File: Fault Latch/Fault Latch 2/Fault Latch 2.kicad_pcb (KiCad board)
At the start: 2 copper layers, 9 parts, among them K103 Fujitsu_FTR-LYAA005x, K104 Fujitsu_FTR-LYAA005x, K105 Fujitsu_FTR-LYAA005x, SW1 SW_Omron_B3FS, SW2 SW_Omron_B3FS, SW3 SW_Omron_B3FS, U105 SFH617A-1, U108 SFH617A-1, U111 SFH617A-1

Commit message: Fault Latch Overhaul
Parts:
- removed SW1, SW2, SW3: SW_Omron_B3FS, Button_Switch_SMD:SW_SPST_Omron_B3FS-100xP
- added C101: 10n, Capacitor_SMD:C_0603_1608Metric_Pad1.08x0.95mm_HandSolder, F.Cu at (94.2, 101.5)
- added C102: 100n, Capacitor_SMD:C_0603_1608Metric_Pad1.08x0.95mm_HandSolder, F.Cu at (88.2, 78.2)
- added C103: 100n, Capacitor_SMD:C_0603_1608Metric_Pad1.08x0.95mm_HandSolder, F.Cu at (95.0, 78.2)
- added C104: 100n, Capacitor_SMD:C_0603_1608Metric_Pad1.08x0.95mm_HandSolder, F.Cu at (81.2, 78.2)
- added C105: 10n, Capacitor_SMD:C_0603_1608Metric_Pad1.08x0.95mm_HandSolder, F.Cu at (94.2, 118.2)
- added C106: 10n, Capacitor_SMD:C_0603_1608Metric_Pad1.08x0.95mm_HandSolder, F.Cu at (93.9, 134.8)
- added C107: 47u, Capacitor_SMD:CP_Elec_6.3x5.4, F.Cu at (133.0, 138.4)
- added C108: 1u, Capacitor_SMD:C_0805_2012Metric_Pad1.18x1.45mm_HandSolder, F.Cu at (115.0, 136.5)
- added C109: 0.33u, Capacitor_SMD:C_0603_1608Metric_Pad1.08x0.95mm_HandSolder, F.Cu at (115.0, 134.5)
- added C110: 100n, Capacitor_SMD:C_0603_1608Metric_Pad1.08x0.95mm_HandSolder, F.Cu at (104.6, 135.5)
- added C111: 100n, Capacitor_SMD:C_0603_1608Metric_Pad1.08x0.95mm_HandSolder, F.Cu at (85.3, 66.4)
- added D101: RED, LED_SMD:LED_0805_2012Metric_Pad1.15x1.40mm_HandSolder, F.Cu at (103.4, 113.0)
- added D102: RED, LED_SMD:LED_0805_2012Metric_Pad1.15x1.40mm_HandSolder, F.Cu at (103.4, 104.0)
- added D103: RED, LED_SMD:LED_0805_2012Metric_Pad1.15x1.40mm_HandSolder, F.Cu at (103.5, 94.8)
- added D104: D_Schottky, Diode_SMD:D_SMA, F.Cu at (135.0, 56.0)
- added D105: D_Schottky, Diode_SMD:D_SMA, F.Cu at (135.5, 67.2)
- added D106: D_Schottky, Diode_SMD:D_SMA, F.Cu at (135.2, 78.8)
- added H101: MountingHole, MountingHole:MountingHole_3.2mm_M3, F.Cu at (80.0, 145.0)
- added H102: MountingHole, MountingHole:MountingHole_3.2mm_M3, F.Cu at (175.0, 145.0)
- added H103: MountingHole, MountingHole:MountingHole_3.2mm_M3, F.Cu at (175.0, 55.0)
- added H104: MountingHole, MountingHole:MountingHole_3.2mm_M3, F.Cu at (80.0, 55.0)
- added PS101: RI-1205S, DC-DC:RI0505S, F.Cu at (114.3, 140.5)
- added Q104: Q_NPN_BEC, Package_TO_SOT_SMD:SOT-23, F.Cu at (90.0, 104.3)
- added Q106: Q_NPN_BEC, Package_TO_SOT_SMD:SOT-23, F.Cu at (94.0, 98.8)
- added Q107: Q_NPN_BEC, Package_TO_SOT_SMD:SOT-23, F.Cu at (89.8, 121.0)
- added Q108: Q_NPN_BEC, Package_TO_SOT_SMD:SOT-23, F.Cu at (94.0, 115.5)
- added Q109: Q_NMOS_GDS, Package_TO_SOT_SMD:TO-252-2, F.Cu at (125.0, 61.2)
- added Q110: Q_NMOS_GDS, Package_TO_SOT_SMD:TO-252-2, F.Cu at (125.1, 70.7)
- added Q111: Q_NMOS_GDS, Package_TO_SOT_SMD:TO-252-2, F.Cu at (125.1, 80.8)
- added Q112: Q_NPN_BEC, Package_TO_SOT_SMD:SOT-23, F.Cu at (89.8, 137.5)
- added Q113: Q_NPN_BEC, Package_TO_SOT_SMD:SOT-23, F.Cu at (93.8, 132.0)
- added R101: 100k, Resistor_SMD:R_0805_2012Metric_Pad1.20x1.40mm_HandSolder, F.Cu at (84.5, 104.3)
- added R102: 10k, Resistor_SMD:R_0805_2012Metric_Pad1.20x1.40mm_HandSolder, F.Cu at (86.8, 104.3)
- added R104: 270R, Resistor_SMD:R_0805_2012Metric_Pad1.20x1.40mm_HandSolder, F.Cu at (100.9, 113.0)
- added R105: 270R, Resistor_SMD:R_0805_2012Metric_Pad1.20x1.40mm_HandSolder, F.Cu at (100.9, 104.0)
- added R106: 1k, Resistor_SMD:R_0805_2012Metric_Pad1.20x1.40mm_HandSolder, F.Cu at (93.2, 104.3)
- added R107: 270R, Resistor_SMD:R_0805_2012Metric_Pad1.20x1.40mm_HandSolder, F.Cu at (101.0, 94.8)
- added R108: 100k, Resistor_SMD:R_0805_2012Metric_Pad1.20x1.40mm_HandSolder, F.Cu at (95.5, 104.3)
- added R109: 1k, Resistor_SMD:R_0805_2012Metric_Pad1.20x1.40mm_HandSolder, F.Cu at (90.8, 97.8)
- added R112: 100k, Resistor_SMD:R_0805_2012Metric_Pad1.20x1.40mm_HandSolder, F.Cu at (84.3, 121.0)
- added R113: 10k, Resistor_SMD:R_0805_2012Metric_Pad1.20x1.40mm_HandSolder, F.Cu at (86.8, 121.0)
- added R114: 1k, Resistor_SMD:R_0805_2012Metric_Pad1.20x1.40mm_HandSolder, F.Cu at (93.0, 121.0)
- added R115: 100k, Resistor_SMD:R_0805_2012Metric_Pad1.20x1.40mm_HandSolder, F.Cu at (95.2, 121.0)
- added R116: 270R, Resistor_SMD:R_0805_2012Metric_Pad1.20x1.40mm_HandSolder, F.Cu at (105.7, 57.4)
- added R117: 270R, Resistor_SMD:R_0805_2012Metric_Pad1.20x1.40mm_HandSolder, F.Cu at (105.7, 67.0)
- added R118: 270R, Resistor_SMD:R_0805_2012Metric_Pad1.20x1.40mm_HandSolder, F.Cu at (105.7, 76.8)
- added R120: 1k, Resistor_SMD:R_0805_2012Metric_Pad1.20x1.40mm_HandSolder, F.Cu at (90.8, 114.5)
- added R121: 10k, Resistor_SMD:R_0805_2012Metric_Pad1.20x1.40mm_HandSolder, F.Cu at (115.3, 57.4)
- added R122: 10k, Resistor_SMD:R_0805_2012Metric_Pad1.20x1.40mm_HandSolder, F.Cu at (115.3, 67.0)
- added R123: 10k, Resistor_SMD:R_0805_2012Metric_Pad1.20x1.40mm_HandSolder, F.Cu at (115.3, 76.8)
- added R124: 100k, Resistor_SMD:R_0805_2012Metric_Pad1.20x1.40mm_HandSolder, F.Cu at (84.0, 137.6)
- added R125: 10k, Resistor_SMD:R_0805_2012Metric_Pad1.20x1.40mm_HandSolder, F.Cu at (86.5, 137.6)
- added R126: 1k, Resistor_SMD:R_0805_2012Metric_Pad1.20x1.40mm_HandSolder, F.Cu at (92.8, 137.5)
- added R127: 100k, Resistor_SMD:R_0805_2012Metric_Pad1.20x1.40mm_HandSolder, F.Cu at (94.9, 137.5)
- added R128: 1k, Resistor_SMD:R_0805_2012Metric_Pad1.20x1.40mm_HandSolder, F.Cu at (90.5, 131.0)
- added R129: 10k, Resistor_SMD:R_0805_2012Metric_Pad1.20x1.40mm_HandSolder, F.Cu at (117.0, 96.8)
- added R131: 2.2k, Resistor_SMD:R_0805_2012Metric_Pad1.20x1.40mm_HandSolder, F.Cu at (117.0, 112.8)
- added R135: 10k, Resistor_SMD:R_0805_2012Metric_Pad1.20x1.40mm_HandSolder, F.Cu at (117.0, 103.8)
- added SW101: SW_Omron_B3FS, Button_Switch_SMD:SW_SPST_Omron_B3FS-100xP, F.Cu at (84.5, 96.8)
- added SW102: SW_Omron_B3FS, Button_Switch_SMD:SW_SPST_Omron_B3FS-100xP, F.Cu at (84.5, 113.2)
- added SW103: SW_Omron_B3FS, Button_Switch_SMD:SW_SPST_Omron_B3FS-100xP, F.Cu at (84.2, 130.0)
- added U101: 641964-1, 641964-1:TE_641964-1, F.Cu at (135.0, 98.8)
- added U102: 74AHC1G00, Package_TO_SOT_SMD:SOT-23-5, F.Cu at (83.0, 81.1)
- added U103: 74AHC1G00, Package_TO_SOT_SMD:SOT-23-5, F.Cu at (90.0, 81.2)
- added U104: 74AHC1G00, Package_TO_SOT_SMD:SOT-23-5, F.Cu at (97.0, 81.2)
- added U105: 641964-1, 641964-1:TE_641964-1, F.Cu at (135.2, 110.1)
- added U106: 74LS279, Package_SO:SOIC-16_3.9x9.9mm_P1.27mm, F.Cu at (91.5, 68.0)
- added U110: 641964-1, 641964-1:TE_641964-1, F.Cu at (169.5, 76.8)
- added U111: 641964-1, 641964-1:TE_641964-1, F.Cu at (169.5, 101.6)
- added U112: 641964-1, 641964-1:TE_641964-1, F.Cu at (169.5, 127.1)
- added U113: 641964-1, 641964-1:TE_641964-1, F.Cu at (135.1, 127.8)
- added U114: SFH617A-1, Package_DIP:DIP-4_W7.62mm, F.Cu at (114.3, 95.8)
- added U115: SFH617A-1, Package_DIP:DIP-4_W7.62mm, F.Cu at (114.3, 114.0)
- added U116: SFH617A-1, Package_DIP:DIP-4_W7.62mm, F.Cu at (114.3, 105.0)
- moved K103 75.0 mm to (133.2, 82.8)
- moved K102 74.7 mm to (133.3, 71.2)
- moved K101 73.5 mm to (132.9, 60.0)
- moved U107 53.5 mm to (106.7, 60.1)
- moved U108 53.0 mm to (106.7, 69.7)
- moved U109 52.7 mm to (106.7, 79.5)
- renumbered K103 to K101, K104 to K102, K105 to K103, U105 to U107, U111 to U109
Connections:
- net GND renamed GNDPWR
- K103 pad 13: unconnected-(K105-Pad13) -> Net-(K103-Pad13)
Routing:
- net +5V: track 0.00 -> 296.7 mm
- net +12V: track 0.00 -> 138.4 mm
- net Net-(K103-Pad13): track 0.00 -> 51.0 mm
- net Net-(K103-Pad14): track 0.00 -> 42.6 mm
- net Net-(K102-Pad13): track 0.00 -> 37.0 mm
- net /BSPD_HV: track 0.00 -> 29.3 mm
- net Net-(K102-Pad14): track 0.00 -> 28.6 mm
- net /IMD_HV: track 0.00 -> 24.6 mm
- net Net-(K101-Pad13): track 0.00 -> 23.6 mm
- net Net-(D106-A): track 0.00 -> 19.1 mm
- net Net-(D105-A): track 0.00 -> 16.7 mm
- net Net-(D104-A): track 0.00 -> 15.9 mm
- net Net-(K101-Pad14): track 0.00 -> 15.8 mm
- net Net-(Q110-G): track 0.00 -> 6.22 mm
- net Net-(Q111-G): track 0.00 -> 6.20 mm
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- added copper zone on F.Cu, net +12V
- added copper zone on F.Cu, net +5V
- added copper zone on B.Cu, net GND
- added copper zone on F.Cu, net GND
- added copper zone on B.Cu, net GNDPWR
- added copper zone on F.Cu, net GNDPWR
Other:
- board outline added: 105 x 100 mm
- board text added: "+12V"
- board text added: "BMS"
- board text added: "BMS_FAULT"
- board text added: "BMS_OUT"
- board text added: "BMS_RESET"
- board text added: "BSPD"
- board text added: "BSPD_FAULT"
- board text added: "BSPD_OUT"
- board text added: "BSPD_RESET"
- board text added: "FAULT LATCH V1.0"
- board text added: "GND"
- board text added: "IMD"
- board text added: "IMD_FAULT"
- board text added: "IMD_OUT"
- board text added: "IMD_RESET"
- board text added: "INPUTS"
- board text added: "OUTPUTS"

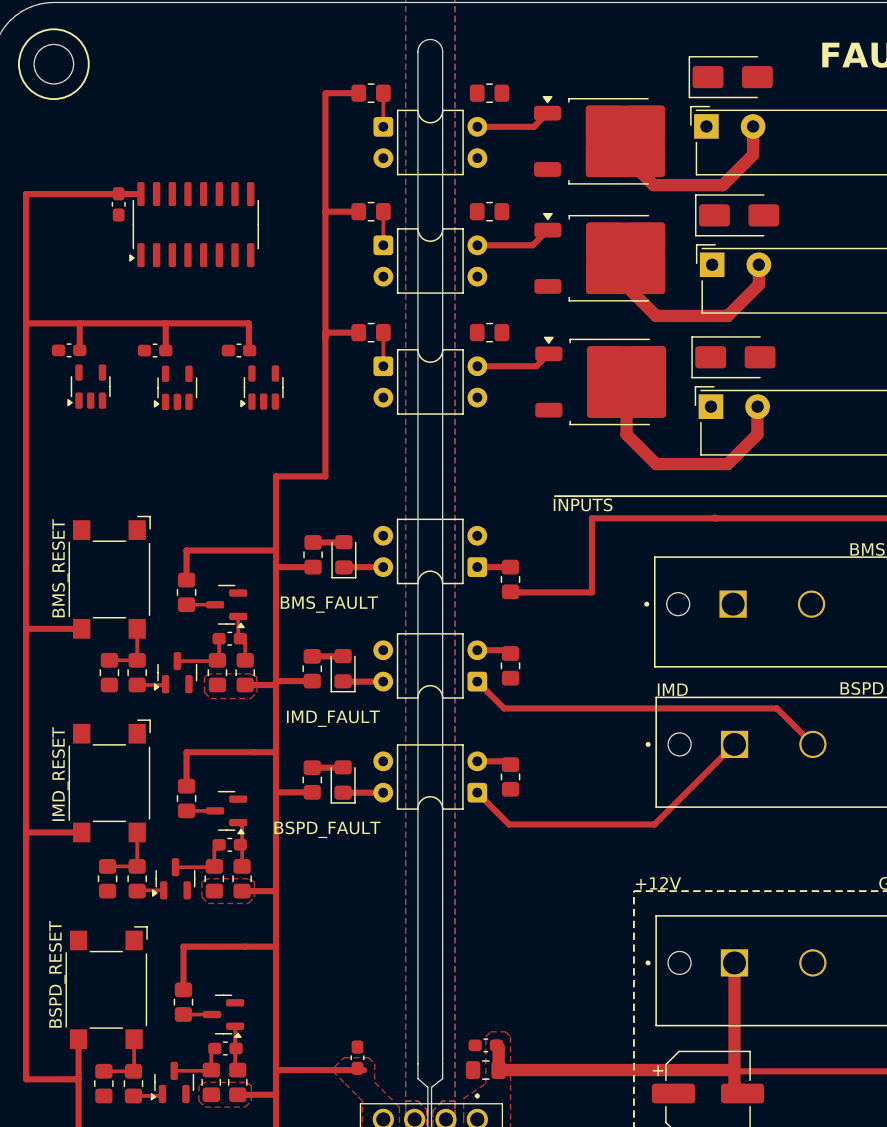
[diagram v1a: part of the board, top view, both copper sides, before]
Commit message: Tried to do traces of Fault Latch
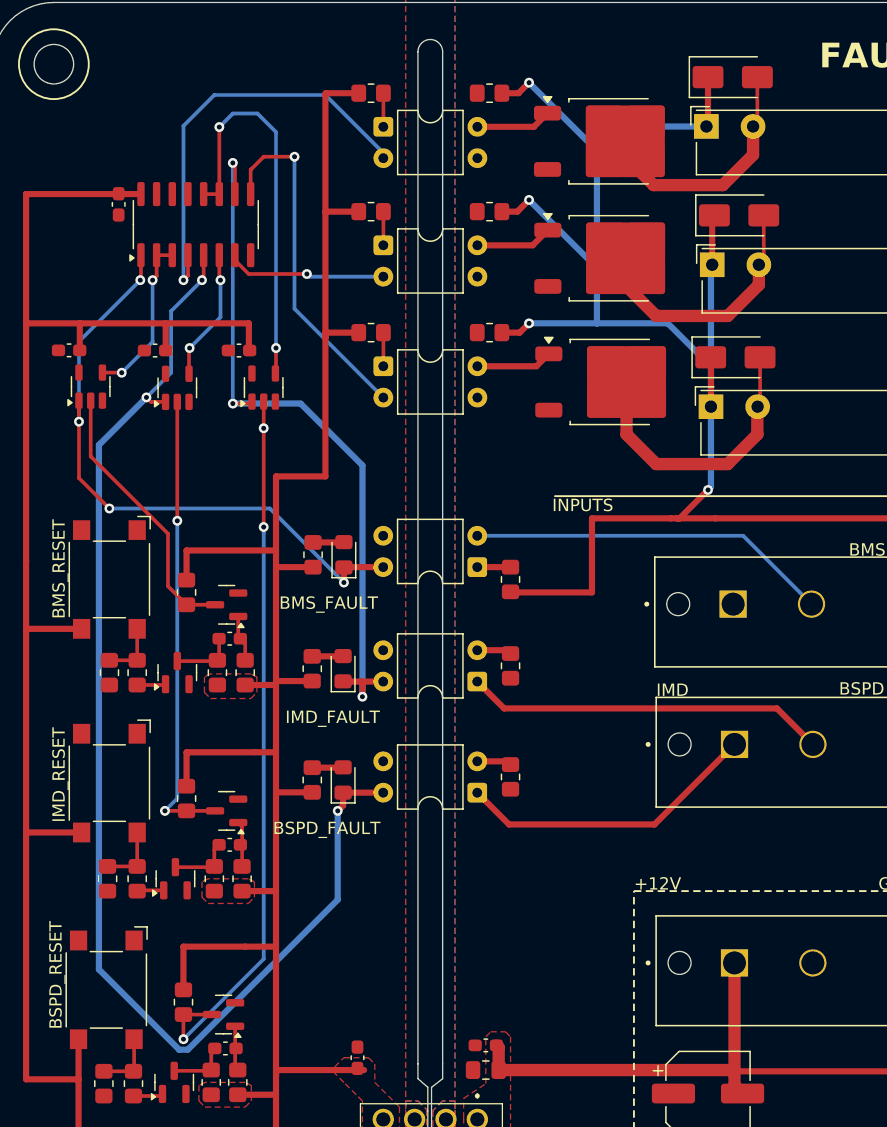
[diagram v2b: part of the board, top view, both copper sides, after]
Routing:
- net /NIMD_LV: track 3.25 -> 102.3 mm, vias 0 -> 3
- net +12V: track 138.4 -> 236.5 mm, vias 0 -> 4
- net /NRESET_BSPD: track 2.31 -> 58.7 mm, vias 0 -> 3
- net /NBPSD_LV: track 3.26 -> 59.5 mm, vias 0 -> 3
- net /NBMS_LV: track 3.20 -> 51.4 mm, vias 0 -> 4
- net /NRESET_IMD: track 2.31 -> 37.6 mm, vias 0 -> 2
- net Net-(U106A-Q): track 0.00 -> 34.3 mm, vias 0 -> 1
- net Net-(U104-Pad4): track 0.00 -> 32.1 mm, vias 0 -> 2
- net /NBMS_HV: track 0.00 -> 29.4 mm
- net Net-(U106C-Q): track 0.00 -> 28.5 mm, vias 0 -> 1
- net /NRESET_BMS: track 2.31 -> 22.1 mm
- net Net-(U102-Pad4): track 0.00 -> 13.5 mm, vias 0 -> 2
- net Net-(U106B-Q): track 0.00 -> 13.0 mm, vias 0 -> 1
- net Net-(U106B-~{S}): track 0.00 -> 10.7 mm, vias 0 -> 2
- net Net-(D105-A): track 16.7 -> 20.9 mm
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
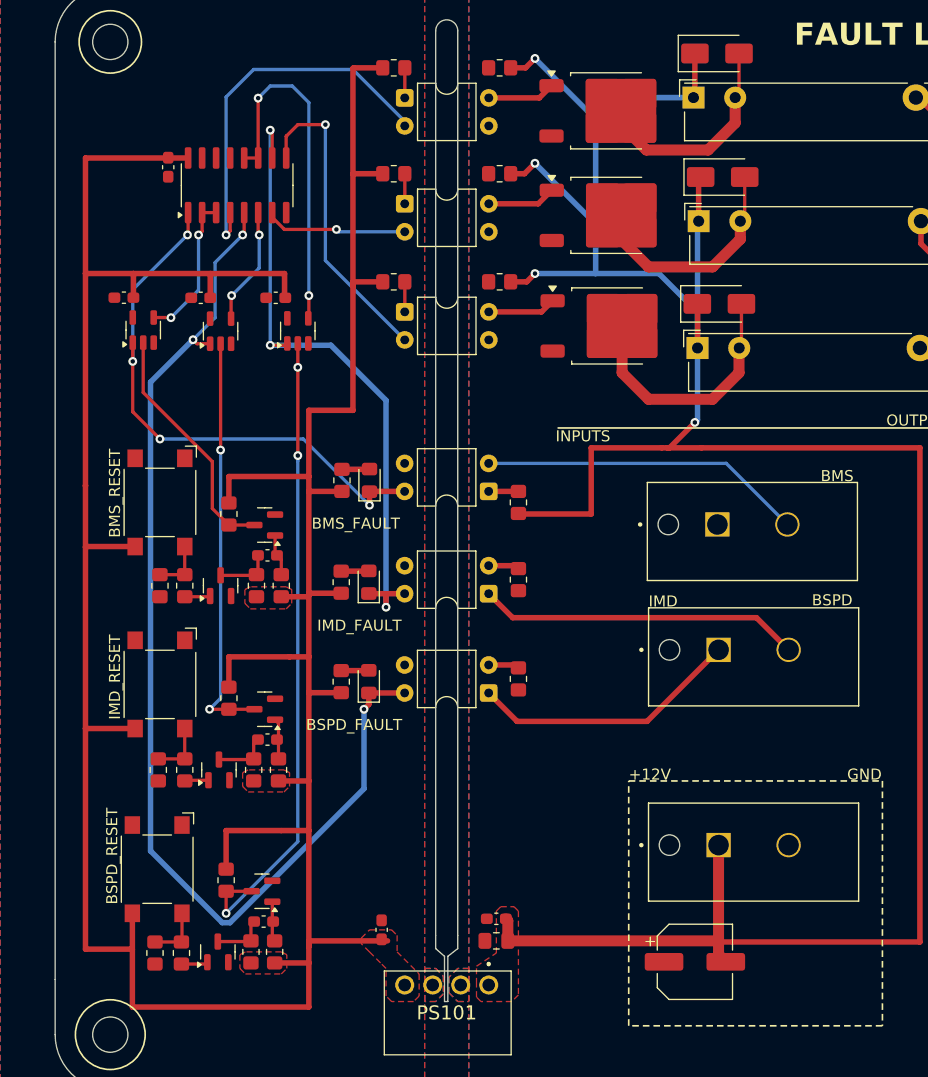
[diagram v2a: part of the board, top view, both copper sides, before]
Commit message: NO ERROR FAULT LATCH.
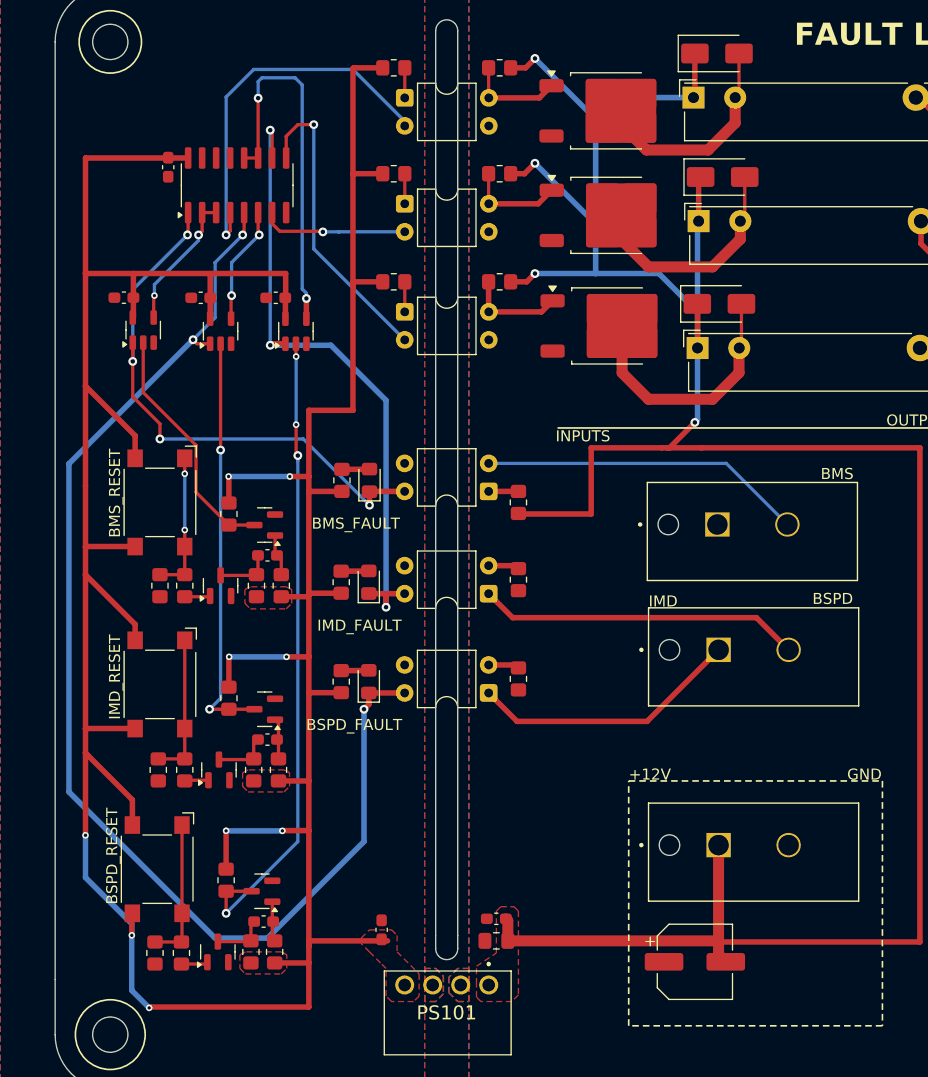
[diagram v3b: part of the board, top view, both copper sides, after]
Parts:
- moved U104 0.18 mm to (96.8, 81.2)
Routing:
- net +5V: track 296.7 -> 322.6 mm, vias 0 -> 9
- net /NIMD_LV: track 102.3 -> 113.6 mm
- net Net-(R124-Pad1): track 5.02 -> 13.0 mm
- net Net-(R112-Pad1): track 5.15 -> 13.2 mm
- net Net-(R101-Pad1): track 4.80 -> 12.8 mm, vias 0 -> 2
- net Net-(Q109-G): track 6.14 -> 8.87 mm
- net Net-(Q111-G): track 6.20 -> 8.93 mm
- net Net-(Q110-G): track 6.22 -> 8.95 mm
- net Net-(U104-Pad4): track 32.1 -> 34.1 mm
- net Net-(U102-Pad4): track 13.5 -> 12.6 mm
- net Net-(U106C-Q): track 28.5 -> 27.8 mm
- net /NRESET_BSPD: vias 3 -> 4
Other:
- outline, holes or cut-outs redrawn
- copper layers 2 -> 4

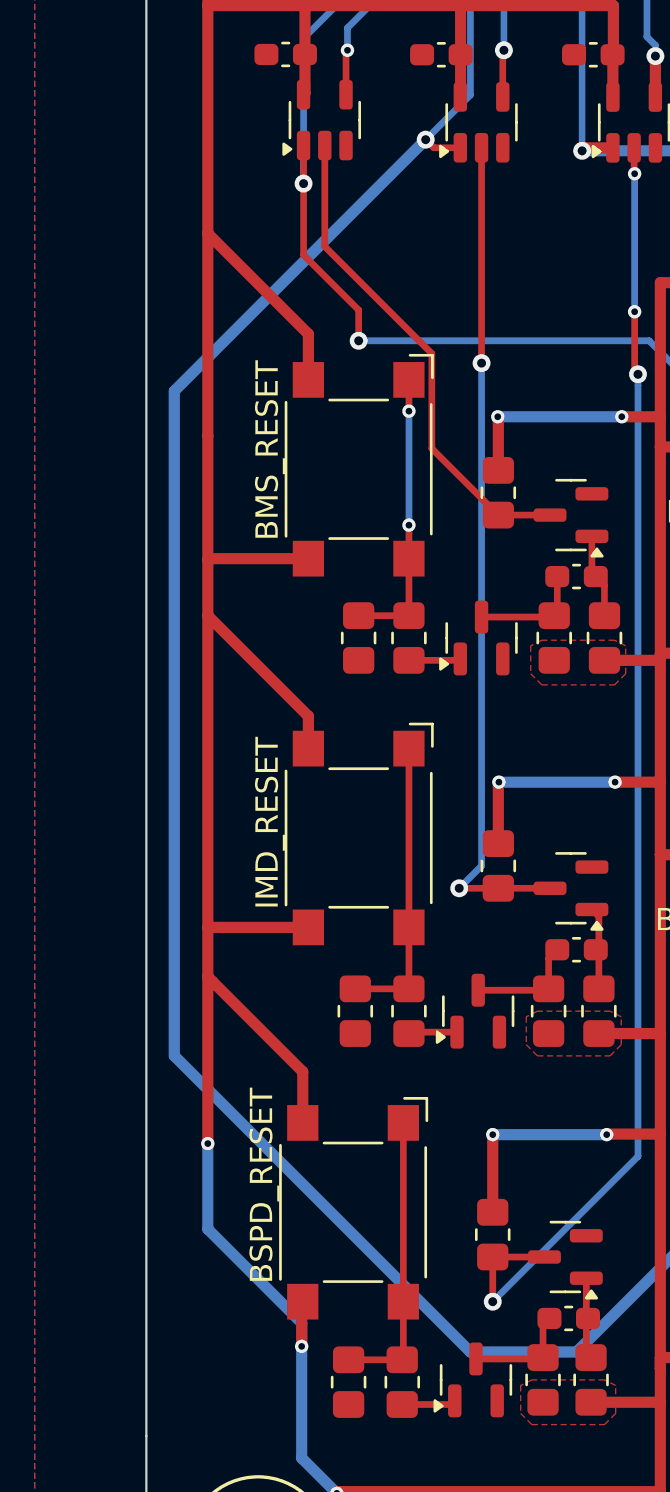
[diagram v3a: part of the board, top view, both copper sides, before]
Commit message: cleaned up fault latch a little
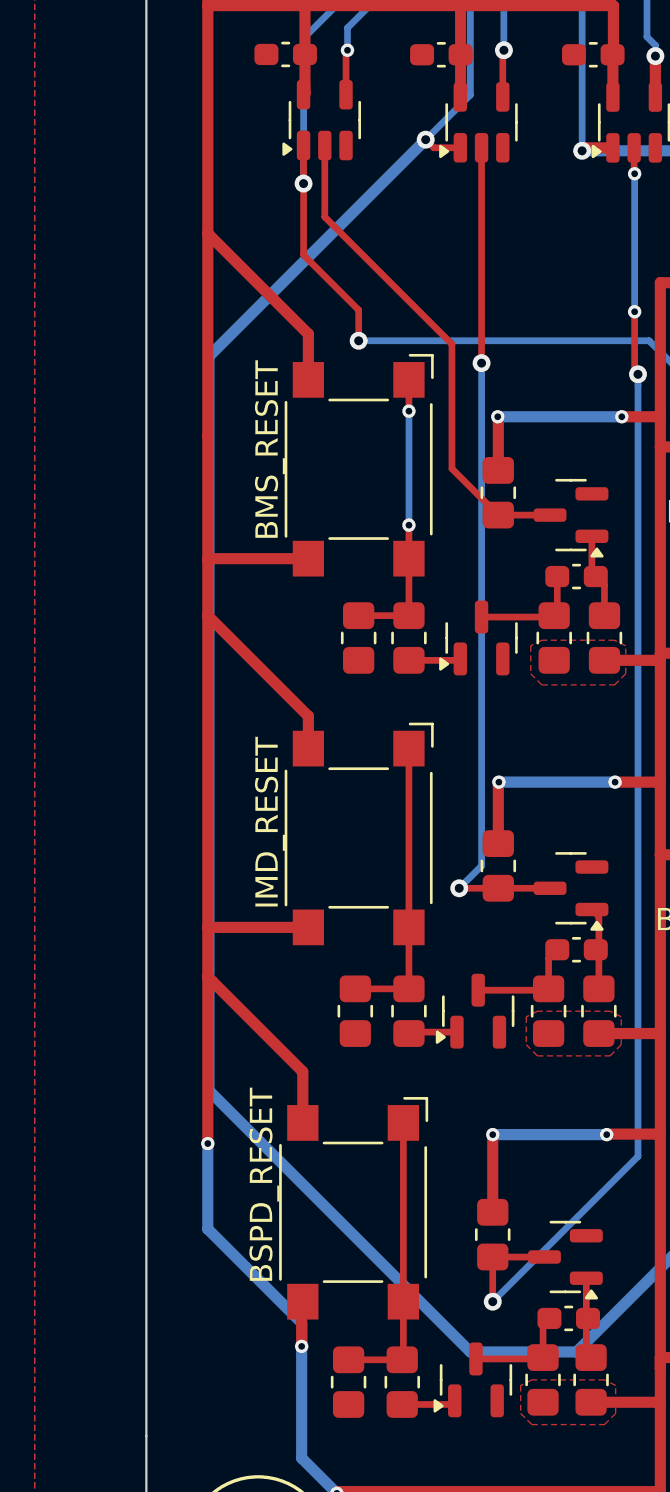
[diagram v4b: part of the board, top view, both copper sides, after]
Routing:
- net /NIMD_LV: track 113.6 -> 112.3 mm
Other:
- copper layers 4 -> 2
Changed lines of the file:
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@@
 	(layers
 		(0 "F.Cu" signal)
-		(4 "In1.Cu" signal)
-		(6 "In2.Cu" signal)
 		(2 "B.Cu" signal)
 		(13 "F.Paste" user)
@@
 			(layer "dielectric 1"
 				(type "core")
-				(thickness 0.480066)
-				(material "FR4")
-				(epsilon_r 4.5)
-				(loss_tangent 0.02)
-			)
-			(layer "In1.Cu"
-				(type "copper")
-				(thickness 0.035)
-			)
-			(layer "dielectric 2"
-				(type "prepreg")
-				(thickness 0.480066)
-				(material "FR4")
-				(epsilon_r 4.5)
-				(loss_tangent 0.02)
-			)
-			(layer "In2.Cu"
-				(type "copper")
-				(thickness 0.035)
-			)
-			(layer "dielectric 3"
-				(type "core")
-				(thickness 0.480066)
+				(thickness 1.510198)
 				(material "FR4")
 				(epsilon_r 4.5)
@@
 	)
 	(segment
-		(start 103 127.5)
-		(end 94.25 136.25)
-		(width 0.5)
-		(layer "B.Cu")
-		(net 11)
-	)
-	(segment
-		(start 103 115.5)
-		(end 103 127.5)
-		(width 0.5)
-		(layer "B.Cu")
-		(net 11)
-	)
-	(segment
 		(start 89.5 75)
 		(end 92 72.5)
@@
 	)
 	(segment
-		(start 76.25 123)
-		(end 76.25 93.25)
+		(start 103 115.5)
+		(end 103 127.5)
 		(width 0.5)
 		(layer "B.Cu")
@@
 	)
 	(segment
-		(start 76.25 93.25)
+		(start 103 127.5)
+		(end 94.25 136.25)
+		(width 0.5)
+		(layer "B.Cu")
+		(net 11)
+	)
+	(segment
+		(start 77.8 91.7)
 		(end 87.5 82)
 		(width 0.5)
@@
 	(segment
 		(start 89.5 136.25)
-		(end 76.25 123)
+		(end 77.8 124.55)
+		(width 0.5)
+		(layer "B.Cu")
+		(net 11)
+	)
+	(segment
+		(start 77.8 124.55)
+		(end 77.8 91.7)
 		(width 0.5)
 		(layer "B.Cu")
@@
 	)
 	(segment
-		(start 82.985 86.783)
-		(end 87.775 91.573)
+		(start 88.675 96.725)
+		(end 90.75 98.8)
 		(width 0.3)
 		(layer "F.Cu")
@@
 	)
 	(segment
-		(start 87.775 95.825)
-		(end 90.75 98.8)
+		(start 90.75 98.8)
+		(end 93.0625 98.8)
 		(width 0.3)
 		(layer "F.Cu")
@@
 	)
 	(segment
-		(start 90.75 98.8)
-		(end 93.0625 98.8)
+		(start 82.985 85.46)
+		(end 88.675 91.15)
 		(width 0.3)
 		(layer "F.Cu")
@@
 	)
 	(segment
-		(start 87.775 91.573)
-		(end 87.775 95.825)
+		(start 82.985 82.2625)
+		(end 82.985 85.46)
 		(width 0.3)
 		(layer "F.Cu")
@@
 	)
 	(segment
-		(start 82.985 82.2625)
-		(end 82.985 86.783)
+		(start 88.675 91.15)
+		(end 88.675 96.725)
 		(width 0.3)
 		(layer "F.Cu")
